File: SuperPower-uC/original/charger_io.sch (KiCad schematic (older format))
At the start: 20 parts, among them J2 Barrel_Jack_Switch, J3 Conn_01x02_Male, Q2 DMP3028LSD, U2 USB-C, U3 IP4220CZ6

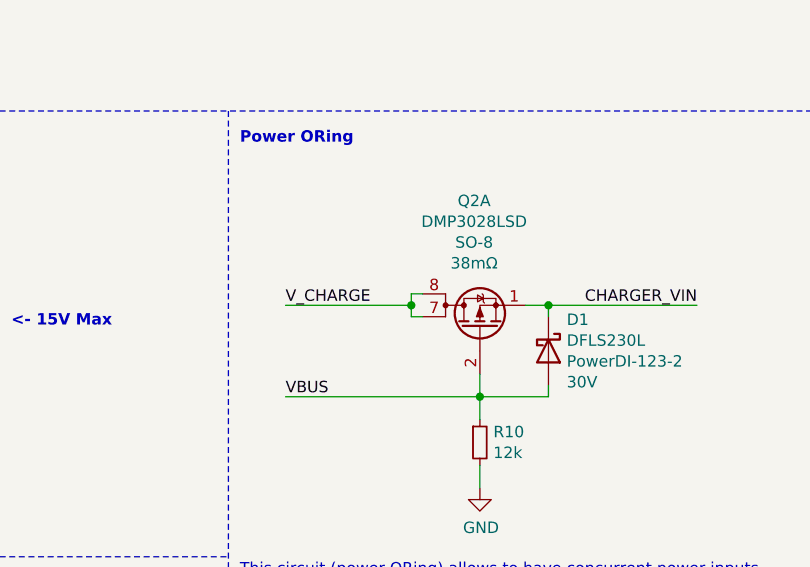
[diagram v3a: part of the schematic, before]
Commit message: Exchanged DMN3018SSD dual mosfet with DMG6402LVT single mosfet and DMN3018SSD dual with DMN3023L single
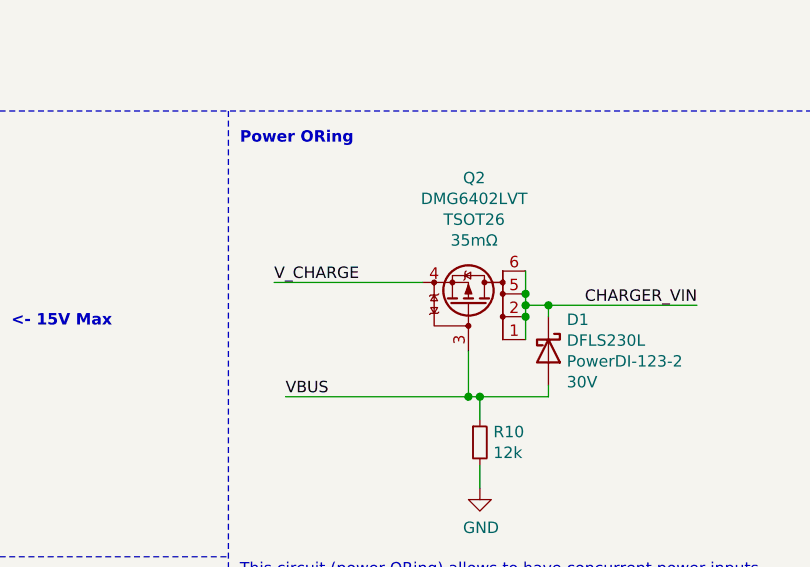
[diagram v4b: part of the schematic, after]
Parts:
- removed Q2: DMP3028LSD, Package_SO:SO-8_3.9x4.9mm_P1.27mm, symbol dmp3028lsd:DMP3028LSD
- added Q2: DMG6402LVT, Package_TO_SOT_SMD:SOT-23-6, symbol dmp2035uvt:DMP2035UVT
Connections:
- net CHARGER_VIN: now also Q2.1 (D), Q2.2 (D), Q2.5 (D), Q2.6 (D)
- net VBUS: now also Q2.3 (G)
- net V_CHARGE: now also Q2.4 (S)
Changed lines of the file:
@@
 	9800 2950 9700 2950
-Wire Wire Line
-	9500 3250 9500 3350
 Wire Wire Line
 	9500 3350 9800 3350
@@
 	9800 2950 10450 2950
 Connection ~ 9800 2950
-Text Label 8650 2950 0    50   ~ 0
+Text Label 8600 2850 0    50   ~ 0
 V_CHARGE
 Text Notes 8450 2250 0    50   ~ 10
@@
 Wire Notes Line
 	5800 5800 8400 5800
-Wire Wire Line
-	8650 2950 9200 2950
 Text Notes 600  650  0    50   ~ 10
 Interface
@@
 	0    -1   -1   0
 $EndComp
-Wire Wire Line
-	9250 2900 9200 2900
-Wire Wire Line
-	9200 2900 9200 2950
-Wire Wire Line
-	9200 3000 9250 3000
-Connection ~ 9200 2950
-Wire Wire Line
-	9200 2950 9200 3000
 Wire Notes Line
 	550  550  2950 550
@@
 	1    1950 1750
 	0    1    1    0
-$EndComp
-$Comp
-L dmp3028lsd:DMP3028LSD Q2
-U 1 1 5FE2DFE6
-P 9500 3050
-F 0 "Q2" V 10057 3075 50  0000 C CNN
-F 1 "DMP3028LSD" V 9966 3075 50  0000 C CNN
-F 2 "Package_SO:SO-8_3.9x4.9mm_P1.27mm" H 9700 2975 50  0001 L CIN
-F 3 "https://www.diodes.com/assets/Datasheets/DMP3028LSD.pdf" V 9500 3050 50  0001 L CNN
-F 4 "Diodes Incorporated" H 9500 3050 50  0001 C CNN "Mfr_name"
-F 5 "DMP3028LSD-13" H 9500 3050 50  0001 C CNN "Mfr_no"
-F 6 "SO-8" V 9875 3075 50  0000 C CNN "Package"
-F 7 "P + P" H 9500 3050 50  0001 C CNN "mos_Type"
-F 8 "30V" H 9500 3050 50  0001 C CNN "mos_VDSS"
-F 9 "38mΩ" V 9784 3075 50  0000 C CNN "mos_RDSon"
-F 10 "4.7A" H 9500 3050 50  0001 C CNN "mos_IDmax"
-F 11 "1-3V" H 9500 3050 50  0001 C CNN "mos_VGSth"
-F 12 "20V" H 9500 3050 50  0001 C CNN "mos_VGSS"
-F 13 "https://octopart.com/dmp3028lsd-13-diodes+inc.-67250487?r=sp" H 9500 3050 50  0001 C CNN "Octopart_link"
-F 14 "-" H 9500 3050 50  0001 C CNN "Farnell_link"
-F 15 "-" H 9500 3050 50  0001 C CNN "Farnell_ref"
-F 16 "2020-12-05" H 9500 3050 50  0001 C CNN "Farnell_check_date"
-F 17 "-" H 9500 3050 50  0001 C CNN "Farnell_price_qt=1"
-F 18 "-" H 9500 3050 50  0001 C CNN "Farnell_price_qt=10"
-F 19 "-" H 9500 3050 50  0001 C CNN "Farnell_price_qt=100"
-F 20 "-" H 9500 3050 50  0001 C CNN "Farnell_price_qt=1000"
-F 21 "-" H 9500 3050 50  0001 C CNN "Farnell_stock"
-F 22 "https://lcsc.com/product-detail/MOSFET_Diodes-Incorporated-DMP3028LSD-13_C397949.html" H 9500 3050 50  0001 C CNN "LCSC_link"
-F 23 "C397949" H 9500 3050 50  0001 C CNN "LCSC_ref"
-F 24 "2020-12-13" H 9500 3050 50  0001 C CNN "LCSC_check_date"
-F 25 "$0.373" H 9500 3050 50  0001 C CNN "LCSC_price_qt=1"
-F 26 "$0.2802" H 9500 3050 50  0001 C CNN "LCSC_price_qt=10"
-F 27 "$0.2475" H 9500 3050 50  0001 C CNN "LCSC_price_qt=100"
-F 28 "$0.2355" H 9500 3050 50  0001 C CNN "LCSC_price_qt=1000"
-F 29 "4,818" H 9500 3050 50  0001 C CNN "LCSC_stock"
-F 30 "https://www.mouser.fr/ProductDetail/Diodes-Incorporated/DMP3028LSD-13?qs=%2Fha2pyFadugUkRnXWzNfjPB%2F2%2FpUVmcBtenJqlz85NswHo6v693iIw%3D%3D" H 9500 3050 50  0001 C CNN "Mouser_link"
-F 31 "621-DMP3028LSD-13" H 9500 3050 50  0001 C CNN "Mouser_ref"
-F 32 "2020-12-13" H 9500 3050 50  0001 C CNN "Mouser_check_date"
-F 33 "$0.564" H 9500 3050 50  0001 C CNN "Mouser_price_qt=1"
-F 34 "$0.469" H 9500 3050 50  0001 C CNN "Mouser_price_qt=10"
-F 35 "$0.328" H 9500 3050 50  0001 C CNN "Mouser_price_qt=100"
-F 36 "$0.242" H 9500 3050 50  0001 C CNN "Mouser_price_qt=1000"
-F 37 "2,855" H 9500 3050 50  0001 C CNN "Mouser_stock"
-F 38 "-" H 9500 3050 50  0001 C CNN "RS_link"
-F 39 "-" H 9500 3050 50  0001 C CNN "RS_ref"
-F 40 "2020-12-05" H 9500 3050 50  0001 C CNN "RS_check_date"
-F 41 "-" H 9500 3050 50  0001 C CNN "RS_price_qt=1"
-F 42 "-" H 9500 3050 50  0001 C CNN "RS_price_qt=10"
-F 43 "-" H 9500 3050 50  0001 C CNN "RS_price_qt=100"
-F 44 "-" H 9500 3050 50  0001 C CNN "RS_price_qt=1000"
-F 45 "-" H 9500 3050 50  0001 C CNN "RS_stock"
-F 46 "TO_CHECK" H 9500 3050 50  0001 C CNN "Status"
-F 47 "1.03" H 9500 3050 50  0001 C CNN "Release_version"
-F 48 "2020-12-21" H 9500 3050 50  0001 C CNN "Release_date"
-F 49 "ManWithNoName" H 9500 3050 50  0001 C CNN "Designer"
-	1    9500 3050
-	0    -1   -1   0
 $EndComp
 $Comp
@@
 	3100 5050 3500 5050
 Wire Wire Line
-	8650 3350 9500 3350
+	8650 3350 9450 3350
 Wire Notes Line
 	8400 2100 8400 5800
@@
 Text Label 1950 1050 2    50   ~ 0
 VBUS
+Wire Wire Line
+	8600 2850 9250 2850
+$Comp
+L dmp2035uvt:DMP2035UVT Q?
+U 1 1 6009A3D3
+P 9450 2950
+AR Path="/5F63A0E9/6009A3D3" Ref="Q?"  Part="1"
+AR Path="/5F63B107/6009A3D3" Ref="Q2"  Part="1"
+F 0 "Q2" V 10007 2975 50  0000 C CNN
+F 1 "DMG6402LVT" V 9916 2975 50  0000 C CNN
+F 2 "Package_TO_SOT_SMD:SOT-23-6" H 9650 3050 50  0001 C CNN
+F 3 "https://www.diodes.com/assets/Datasheets/DMP2035UVT.pdf" H 9450 2950 50  0001 C CNN
+F 4 "Diodes Incorporated" H 9450 2950 50  0001 C CNN "Mfr_name"
+F 5 "DMP2035UVT-7" H 9450 2950 50  0001 C CNN "Mfr_no"
+F 6 "TSOT26" V 9825 2975 50  0000 C CNN "Package"
+F 7 "P" H 9450 2950 50  0001 C CNN "mos_Type"
+F 8 "-20V" H 9450 2950 50  0001 C CNN "mos_VDSS"
+F 9 "35mΩ" V 9734 2975 50  0000 C CNN "mos_RDSon"
+F 10 "-6.0A" H 9450 2950 50  0001 C CNN "mos_IDmax"
+F 11 "-0.4V_to_-1.5V" H 9450 2950 50  0001 C CNN "mos_VGSth"
+F 12 "12V" H 9450 2950 50  0001 C CNN "mos_VGSS"
+F 13 "https://octopart.com/dmp2035uvt-7-diodes+inc.-21789379?r=sp" H 9450 2950 50  0001 C CNN "Octopart_link"
+F 14 "https://fr.farnell.com/diodes-inc/dmp2035uvt-7/mosfet-canal-p-20v-6a-150-1-2w/dp/3405183?st=dmp2035uvt" H 9450 2950 50  0001 C CNN "Farnell_link"
+F 15 "3405183" H 9450 2950 50  0001 C CNN "Farnell_ref"
+F 16 "2020-12-11" H 9450 2950 50  0001 C CNN "Farnell_check_date"
+F 17 "-" H 9450 2950 50  0001 C CNN "Farnell_price_qt=1"
+F 18 "0,52 €" H 9450 2950 50  0001 C CNN "Farnell_price_qt=10"
+F 19 "0,238 €" H 9450 2950 50  0001 C CNN "Farnell_price_qt=100"
+F 20 "0,141 €" H 9450 2950 50  0001 C CNN "Farnell_price_qt=1000"
+F 21 "2,890" H 9450 2950 50  0001 C CNN "Farnell_stock"
+F 22 "https://lcsc.com/product-detail/MOSFET_Diodes-Incorporated-DMP2035UVT-7_C260934.html" H 9450 2950 50  0001 C CNN "LCSC_link"
+F 23 "C260934" H 9450 2950 50  0001 C CNN "LCSC_ref"
+F 24 "2020-12-11" H 9450 2950 50  0001 C CNN "LCSC_check_date"
+F 25 "-" H 9450 2950 50  0001 C CNN "LCSC_price_qt=1"
+F 26 "$0.1253" H 9450 2950 50  0001 C CNN "LCSC_price_qt=10"
+F 27 "$0.0932" H 9450 2950 50  0001 C CNN "LCSC_price_qt=100"
+F 28 "$0.0814" H 9450 2950 50  0001 C CNN "LCSC_price_qt=1000"
+F 29 "7,535" H 9450 2950 50  0001 C CNN "LCSC_stock"
+F 30 "https://eu.mouser.com/ProductDetail/Diodes-Incorporated/DMP2035UVT-7?qs=F5djdNSOT4Y3SEHDwWTQ6g%3D%3D" H 9450 2950 50  0001 C CNN "Mouser_link"
+F 31 "621-DMP2035UVT-7" H 9450 2950 50  0001 C CNN "Mouser_ref"
+F 32 "2020-12-11" H 9450 2950 50  0001 C CNN "Mouser_check_date"
+F 33 "$0.474" H 9450 2950 50  0001 C CNN "Mouser_price_qt=1"
+F 34 "$0.346" H 9450 2950 50  0001 C CNN "Mouser_price_qt=10"
+F 35 "$0.215" H 9450 2950 50  0001 C CNN "Mouser_price_qt=100"
+F 36 "$0.137" H 9450 2950 50  0001 C CNN "Mouser_price_qt=1000"
+F 37 "19,684" H 9450 2950 50  0001 C CNN "Mouser_stock"
+F 38 "-" H 9450 2950 50  0001 C CNN "RS_link"
+F 39 "-" H 9450 2950 50  0001 C CNN "RS_ref"
+F 40 "2020-12-11" H 9450 2950 50  0001 C CNN "RS_check_date"
+F 41 "-" H 9450 2950 50  0001 C CNN "RS_price_qt=1"
+F 42 "-" H 9450 2950 50  0001 C CNN "RS_price_qt=10"
+F 43 "-" H 9450 2950 50  0001 C CNN "RS_price_qt=100"
+F 44 "-" H 9450 2950 50  0001 C CNN "RS_price_qt=1000"
+F 45 "-" H 9450 2950 50  0001 C CNN "RS_stock"
+F 46 "TO_CHECK" H 9450 2950 50  0001 C CNN "Status"
+F 47 "1.01" H 9450 2950 50  0001 C CNN "Release_version"
+F 48 "2020-12-18" H 9450 2950 50  0001 C CNN "Release_date"
+F 49 "ManWithNoName" H 9450 2950 50  0001 C CNN "Designer"
+	1    9450 2950
+	0    1    -1   0
+$EndComp
+Wire Wire Line
+	9450 3150 9450 3350
+Connection ~ 9450 3350
+Wire Wire Line
+	9450 3350 9500 3350
+Wire Wire Line
+	9700 3100 9700 3000
+Connection ~ 9700 2900
+Wire Wire Line
+	9700 2900 9700 2800
+Connection ~ 9700 2950
+Wire Wire Line
+	9700 2950 9700 2900
+Connection ~ 9700 3000
+Wire Wire Line
+	9700 3000 9700 2950
 $EndSCHEMATC

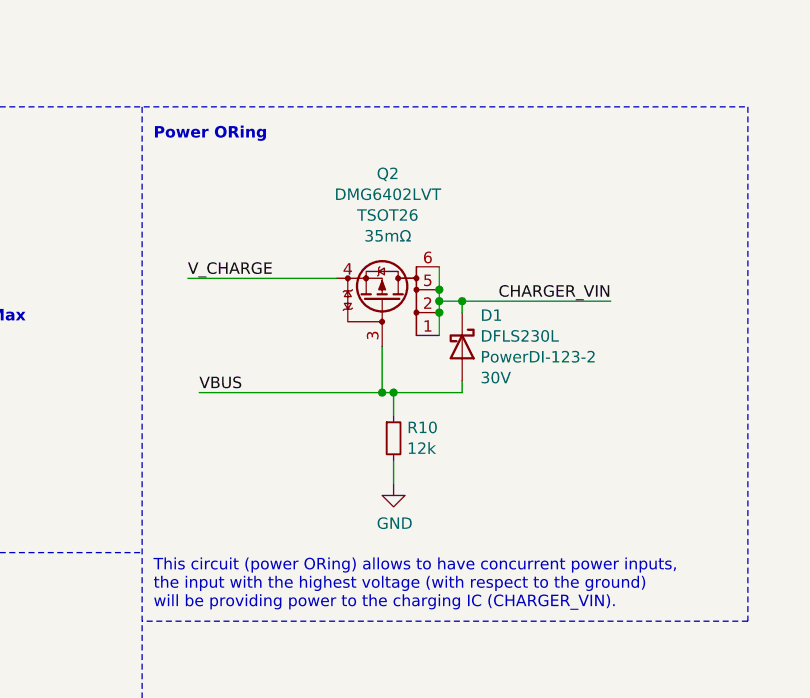
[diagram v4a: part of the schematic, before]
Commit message: Reverted the change of the DMP3028LSD
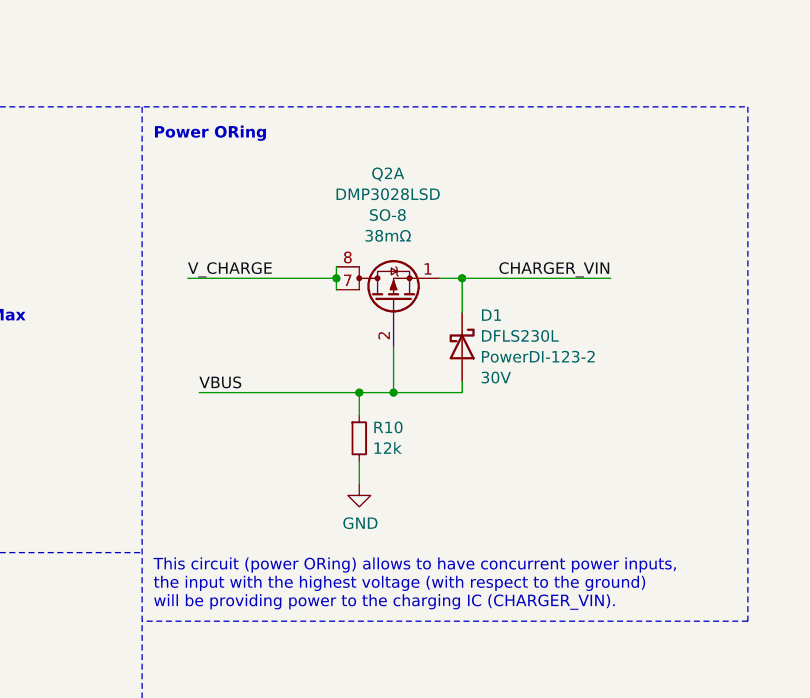
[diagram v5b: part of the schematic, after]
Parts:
- removed Q2: DMG6402LVT, Package_TO_SOT_SMD:SOT-23-6, symbol dmp2035uvt:DMP2035UVT
- added Q2: DMP3028LSD, Package_SO:SO-8_3.9x4.9mm_P1.27mm, symbol dmp3028lsd:DMP3028LSD
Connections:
- net CHARGER_VIN: now also Q2.1 (S)
- net VBUS: now also Q2.2 (G)
- net V_CHARGE: now also Q2.7 (D), Q2.8 (D)
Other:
- moved on the sheet: R10
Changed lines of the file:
@@
 L Device:R_Small R?
 U 1 1 5FA2BEE4
-P 9500 3550
+P 9350 3550
 AR Path="/5F639F48/5FA2BEE4" Ref="R?"  Part="1"
 AR Path="/5F63B107/5FA2BEE4" Ref="R10"  Part="1"
-F 0 "R10" H 9559 3596 50  0000 L CNN
-F 1 "12k" H 9559 3505 50  0000 L CNN
-F 2 "Resistor_SMD:R_0603_1608Metric" H 9500 3550 50  0001 C CNN
-F 3 "~" H 9500 3550 50  0001 C CNN
-	1    9500 3550
+F 0 "R10" H 9409 3596 50  0000 L CNN
+F 1 "12k" H 9409 3505 50  0000 L CNN
+F 2 "Resistor_SMD:R_0603_1608Metric" H 9350 3550 50  0001 C CNN
+F 3 "~" H 9350 3550 50  0001 C CNN
+	1    9350 3550
 	1    0    0    -1
 $EndComp
@@
 L power:GND #PWR?
 U 1 1 5FA2BEFE
-P 9500 3750
+P 9350 3750
 AR Path="/5F639F48/5FA2BEFE" Ref="#PWR?"  Part="1"
 AR Path="/5F63B107/5FA2BEFE" Ref="#PWR021"  Part="1"
-F 0 "#PWR021" H 9500 3500 50  0001 C CNN
-F 1 "GND" H 9505 3577 50  0000 C CNN
-F 2 "" H 9500 3750 50  0001 C CNN
-F 3 "" H 9500 3750 50  0001 C CNN
-	1    9500 3750
-	1    0    0    -1
-$EndComp
-Wire Wire Line
-	9500 3750 9500 3650
-Wire Wire Line
-	9800 3000 9800 2950
-Wire Wire Line
-	9800 2950 9700 2950
-Wire Wire Line
-	9500 3350 9800 3350
+F 0 "#PWR021" H 9350 3500 50  0001 C CNN
+F 1 "GND" H 9355 3577 50  0000 C CNN
+F 2 "" H 9350 3750 50  0001 C CNN
+F 3 "" H 9350 3750 50  0001 C CNN
+	1    9350 3750
+	1    0    0    -1
+$EndComp
+Wire Wire Line
+	9350 3750 9350 3650
 Wire Wire Line
 	9800 3350 9800 3300
-Connection ~ 9500 3350
-Wire Wire Line
-	9500 3350 9500 3450
-Text Label 10450 2950 2    50   ~ 0
+Wire Wire Line
+	9350 3350 9350 3450
+Text Label 10450 2850 2    50   ~ 0
 CHARGER_VIN
-Wire Wire Line
-	9800 2950 10450 2950
-Connection ~ 9800 2950
 Text Label 8600 2850 0    50   ~ 0
 V_CHARGE
@@
 Wire Wire Line
 	3100 5050 3500 5050
-Wire Wire Line
-	8650 3350 9450 3350
 Wire Notes Line
 	8400 2100 8400 5800
@@
 	8600 2850 9250 2850
 $Comp
-L dmp2035uvt:DMP2035UVT Q?
-U 1 1 6009A3D3
-P 9450 2950
-AR Path="/5F63A0E9/6009A3D3" Ref="Q?"  Part="1"
-AR Path="/5F63B107/6009A3D3" Ref="Q2"  Part="1"
-F 0 "Q2" V 10007 2975 50  0000 C CNN
-F 1 "DMG6402LVT" V 9916 2975 50  0000 C CNN
-F 2 "Package_TO_SOT_SMD:SOT-23-6" H 9650 3050 50  0001 C CNN
-F 3 "https://www.diodes.com/assets/Datasheets/DMP2035UVT.pdf" H 9450 2950 50  0001 C CNN
-F 4 "Diodes Incorporated" H 9450 2950 50  0001 C CNN "Mfr_name"
-F 5 "DMP2035UVT-7" H 9450 2950 50  0001 C CNN "Mfr_no"
-F 6 "TSOT26" V 9825 2975 50  0000 C CNN "Package"
-F 7 "P" H 9450 2950 50  0001 C CNN "mos_Type"
-F 8 "-20V" H 9450 2950 50  0001 C CNN "mos_VDSS"
-F 9 "35mΩ" V 9734 2975 50  0000 C CNN "mos_RDSon"
-F 10 "-6.0A" H 9450 2950 50  0001 C CNN "mos_IDmax"
-F 11 "-0.4V_to_-1.5V" H 9450 2950 50  0001 C CNN "mos_VGSth"
-F 12 "12V" H 9450 2950 50  0001 C CNN "mos_VGSS"
-F 13 "https://octopart.com/dmp2035uvt-7-diodes+inc.-21789379?r=sp" H 9450 2950 50  0001 C CNN "Octopart_link"
-F 14 "https://fr.farnell.com/diodes-inc/dmp2035uvt-7/mosfet-canal-p-20v-6a-150-1-2w/dp/3405183?st=dmp2035uvt" H 9450 2950 50  0001 C CNN "Farnell_link"
-F 15 "3405183" H 9450 2950 50  0001 C CNN "Farnell_ref"
-F 16 "2020-12-11" H 9450 2950 50  0001 C CNN "Farnell_check_date"
-F 17 "-" H 9450 2950 50  0001 C CNN "Farnell_price_qt=1"
-F 18 "0,52 €" H 9450 2950 50  0001 C CNN "Farnell_price_qt=10"
-F 19 "0,238 €" H 9450 2950 50  0001 C CNN "Farnell_price_qt=100"
-F 20 "0,141 €" H 9450 2950 50  0001 C CNN "Farnell_price_qt=1000"
-F 21 "2,890" H 9450 2950 50  0001 C CNN "Farnell_stock"
-F 22 "https://lcsc.com/product-detail/MOSFET_Diodes-Incorporated-DMP2035UVT-7_C260934.html" H 9450 2950 50  0001 C CNN "LCSC_link"
-F 23 "C260934" H 9450 2950 50  0001 C CNN "LCSC_ref"
-F 24 "2020-12-11" H 9450 2950 50  0001 C CNN "LCSC_check_date"
-F 25 "-" H 9450 2950 50  0001 C CNN "LCSC_price_qt=1"
-F 26 "$0.1253" H 9450 2950 50  0001 C CNN "LCSC_price_qt=10"
-F 27 "$0.0932" H 9450 2950 50  0001 C CNN "LCSC_price_qt=100"
-F 28 "$0.0814" H 9450 2950 50  0001 C CNN "LCSC_price_qt=1000"
-F 29 "7,535" H 9450 2950 50  0001 C CNN "LCSC_stock"
-F 30 "https://eu.mouser.com/ProductDetail/Diodes-Incorporated/DMP2035UVT-7?qs=F5djdNSOT4Y3SEHDwWTQ6g%3D%3D" H 9450 2950 50  0001 C CNN "Mouser_link"
-F 31 "621-DMP2035UVT-7" H 9450 2950 50  0001 C CNN "Mouser_ref"
-F 32 "2020-12-11" H 9450 2950 50  0001 C CNN "Mouser_check_date"
-F 33 "$0.474" H 9450 2950 50  0001 C CNN "Mouser_price_qt=1"
-F 34 "$0.346" H 9450 2950 50  0001 C CNN "Mouser_price_qt=10"
-F 35 "$0.215" H 9450 2950 50  0001 C CNN "Mouser_price_qt=100"
-F 36 "$0.137" H 9450 2950 50  0001 C CNN "Mouser_price_qt=1000"
-F 37 "19,684" H 9450 2950 50  0001 C CNN "Mouser_stock"
-F 38 "-" H 9450 2950 50  0001 C CNN "RS_link"
-F 39 "-" H 9450 2950 50  0001 C CNN "RS_ref"
-F 40 "2020-12-11" H 9450 2950 50  0001 C CNN "RS_check_date"
-F 41 "-" H 9450 2950 50  0001 C CNN "RS_price_qt=1"
-F 42 "-" H 9450 2950 50  0001 C CNN "RS_price_qt=10"
-F 43 "-" H 9450 2950 50  0001 C CNN "RS_price_qt=100"
-F 44 "-" H 9450 2950 50  0001 C CNN "RS_price_qt=1000"
-F 45 "-" H 9450 2950 50  0001 C CNN "RS_stock"
-F 46 "TO_CHECK" H 9450 2950 50  0001 C CNN "Status"
-F 47 "1.01" H 9450 2950 50  0001 C CNN "Release_version"
-F 48 "2020-12-18" H 9450 2950 50  0001 C CNN "Release_date"
-F 49 "ManWithNoName" H 9450 2950 50  0001 C CNN "Designer"
-	1    9450 2950
-	0    1    -1   0
-$EndComp
-Wire Wire Line
-	9450 3150 9450 3350
-Connection ~ 9450 3350
-Wire Wire Line
-	9450 3350 9500 3350
-Wire Wire Line
-	9700 3100 9700 3000
-Connection ~ 9700 2900
-Wire Wire Line
-	9700 2900 9700 2800
-Connection ~ 9700 2950
-Wire Wire Line
-	9700 2950 9700 2900
-Connection ~ 9700 3000
-Wire Wire Line
-	9700 3000 9700 2950
+L dmp3028lsd:DMP3028LSD Q2
+U 1 1 6007EF0E
+P 9500 2950
+F 0 "Q2" V 10057 2975 50  0000 C CNN
+F 1 "DMP3028LSD" V 9966 2975 50  0000 C CNN
+F 2 "Package_SO:SO-8_3.9x4.9mm_P1.27mm" H 9700 2875 50  0001 L CIN
+F 3 "https://www.diodes.com/assets/Datasheets/DMP3028LSD.pdf" V 9500 2950 50  0001 L CNN
+F 4 "Diodes Incorporated" H 9500 2950 50  0001 C CNN "Mfr_name"
+F 5 "DMP3028LSD-13" H 9500 2950 50  0001 C CNN "Mfr_no"
+F 6 "SO-8" V 9875 2975 50  0000 C CNN "Package"
+F 7 "P + P" H 9500 2950 50  0001 C CNN "mos_Type"
+F 8 "30V" H 9500 2950 50  0001 C CNN "mos_VDSS"
+F 9 "38mΩ" V 9784 2975 50  0000 C CNN "mos_RDSon"
+F 10 "4.7A" H 9500 2950 50  0001 C CNN "mos_IDmax"
+F 11 "1-3V" H 9500 2950 50  0001 C CNN "mos_VGSth"
+F 12 "20V" H 9500 2950 50  0001 C CNN "mos_VGSS"
+F 13 "https://octopart.com/dmp3028lsd-13-diodes+inc.-67250487?r=sp" H 9500 2950 50  0001 C CNN "Octopart_link"
+F 14 "-" H 9500 2950 50  0001 C CNN "Farnell_link"
+F 15 "-" H 9500 2950 50  0001 C CNN "Farnell_ref"
+F 16 "2020-12-05" H 9500 2950 50  0001 C CNN "Farnell_check_date"
+F 17 "-" H 9500 2950 50  0001 C CNN "Farnell_price_qt=1"
+F 18 "-" H 9500 2950 50  0001 C CNN "Farnell_price_qt=10"
+F 19 "-" H 9500 2950 50  0001 C CNN "Farnell_price_qt=100"
+F 20 "-" H 9500 2950 50  0001 C CNN "Farnell_price_qt=1000"
+F 21 "-" H 9500 2950 50  0001 C CNN "Farnell_stock"
+F 22 "https://lcsc.com/product-detail/MOSFET_Diodes-Incorporated-DMP3028LSD-13_C397949.html" H 9500 2950 50  0001 C CNN "LCSC_link"
+F 23 "C397949" H 9500 2950 50  0001 C CNN "LCSC_ref"
+F 24 "2020-12-13" H 9500 2950 50  0001 C CNN "LCSC_check_date"
+F 25 "$0.373" H 9500 2950 50  0001 C CNN "LCSC_price_qt=1"
+F 26 "$0.2802" H 9500 2950 50  0001 C CNN "LCSC_price_qt=10"
+F 27 "$0.2475" H 9500 2950 50  0001 C CNN "LCSC_price_qt=100"
+F 28 "$0.2355" H 9500 2950 50  0001 C CNN "LCSC_price_qt=1000"
+F 29 "4,818" H 9500 2950 50  0001 C CNN "LCSC_stock"
+F 30 "https://www.mouser.fr/ProductDetail/Diodes-Incorporated/DMP3028LSD-13?qs=%2Fha2pyFadugUkRnXWzNfjPB%2F2%2FpUVmcBtenJqlz85NswHo6v693iIw%3D%3D" H 9500 2950 50  0001 C CNN "Mouser_link"
+F 31 "621-DMP3028LSD-13" H 9500 2950 50  0001 C CNN "Mouser_ref"
+F 32 "2020-12-13" H 9500 2950 50  0001 C CNN "Mouser_check_date"
+F 33 "$0.564" H 9500 2950 50  0001 C CNN "Mouser_price_qt=1"
+F 34 "$0.469" H 9500 2950 50  0001 C CNN "Mouser_price_qt=10"
+F 35 "$0.328" H 9500 2950 50  0001 C CNN "Mouser_price_qt=100"
+F 36 "$0.242" H 9500 2950 50  0001 C CNN "Mouser_price_qt=1000"
+F 37 "2,855" H 9500 2950 50  0001 C CNN "Mouser_stock"
+F 38 "-" H 9500 2950 50  0001 C CNN "RS_link"
+F 39 "-" H 9500 2950 50  0001 C CNN "RS_ref"
+F 40 "2020-12-05" H 9500 2950 50  0001 C CNN "RS_check_date"
+F 41 "-" H 9500 2950 50  0001 C CNN "RS_price_qt=1"
+F 42 "-" H 9500 2950 50  0001 C CNN "RS_price_qt=10"
+F 43 "-" H 9500 2950 50  0001 C CNN "RS_price_qt=100"
+F 44 "-" H 9500 2950 50  0001 C CNN "RS_price_qt=1000"
+F 45 "-" H 9500 2950 50  0001 C CNN "RS_stock"
+F 46 "TO_CHECK" H 9500 2950 50  0001 C CNN "Status"
+F 47 "1.03" H 9500 2950 50  0001 C CNN "Release_version"
+F 48 "2020-12-21" H 9500 2950 50  0001 C CNN "Release_date"
+F 49 "ManWithNoName" H 9500 2950 50  0001 C CNN "Designer"
+	1    9500 2950
+	0    -1   -1   0
+$EndComp
+Wire Wire Line
+	8650 3350 9350 3350
+Connection ~ 9350 3350
+Wire Wire Line
+	9350 3350 9500 3350
+Wire Wire Line
+	9500 3350 9500 3150
+Connection ~ 9500 3350
+Wire Wire Line
+	9500 3350 9800 3350
+Wire Wire Line
+	9700 2850 9800 2850
+Wire Wire Line
+	9800 2850 9800 3000
+Connection ~ 9800 2850
+Wire Wire Line
+	9800 2850 10450 2850
+Wire Wire Line
+	9250 2900 9250 2850
+Connection ~ 9250 2850
+Wire Wire Line
+	9250 2850 9250 2800
 $EndSCHEMATC
